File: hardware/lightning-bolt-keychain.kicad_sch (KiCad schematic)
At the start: 8 parts, among them SW1 SPST

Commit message: Repair KiCad PCB and update parts notes
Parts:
- BT1: value CR2032 -> CR1220/CR1225; symbol Battery:Battery_Cell -> Device:Battery_Cell
- SW1: footprint Button_Switch_SMD:SW_SPST_EVQP2 -> Button_Switch_SMD:SW_SPST_EVQP2_ShortPushTravel_H2.1mm
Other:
- note added: "Simple 12 mm coin-cell keychain circuit: BT1 -> SW1 -> three resistor/LED branches."
- note removed: "Simple CR2032 keychain circuit: BT1 -> SW1 -> three resistor/LED branches."
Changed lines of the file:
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@@
     (rev "A")
     (company "Open hardware concept")
-    (comment 1 "CR2032 powered amber LED keychain")
+    (comment 1 "12mm coin-cell powered amber LED keychain")
   )
   (junction (at 74.93 67.31) (diameter 0) (color 0 0 0 0)
@@
     (stroke (width 0) (type default))
   )
-  (wire (pts (xy 74.93 67.31) (xy 86.36 67.31))
+  (wire (pts (xy 74.93 67.31) (xy 87.63 67.31))
     (stroke (width 0) (type default))
   )
@@
     (stroke (width 0) (type default))
   )
-  (wire (pts (xy 74.93 85.09) (xy 86.36 85.09))
+  (wire (pts (xy 74.93 85.09) (xy 87.63 85.09))
     (stroke (width 0) (type default))
   )
@@
     (stroke (width 0) (type default))
   )
-  (wire (pts (xy 74.93 102.87) (xy 86.36 102.87))
+  (wire (pts (xy 74.93 102.87) (xy 87.63 102.87))
     (stroke (width 0) (type default))
   )
-  (wire (pts (xy 96.52 67.31) (xy 106.68 67.31))
+  (wire (pts (xy 95.25 67.31) (xy 107.95 67.31))
     (stroke (width 0) (type default))
   )
-  (wire (pts (xy 96.52 85.09) (xy 106.68 85.09))
+  (wire (pts (xy 95.25 85.09) (xy 107.95 85.09))
     (stroke (width 0) (type default))
   )
-  (wire (pts (xy 96.52 102.87) (xy 106.68 102.87))
+  (wire (pts (xy 95.25 102.87) (xy 107.95 102.87))
     (stroke (width 0) (type default))
   )
-  (wire (pts (xy 116.84 67.31) (xy 116.84 102.87))
+  (wire (pts (xy 115.57 67.31) (xy 115.57 102.87))
     (stroke (width 0) (type default))
   )
-  (wire (pts (xy 106.68 67.31) (xy 116.84 67.31))
+  (wire (pts (xy 115.57 67.31) (xy 115.57 67.31))
     (stroke (width 0) (type default))
   )
-  (wire (pts (xy 106.68 85.09) (xy 116.84 85.09))
+  (wire (pts (xy 115.57 85.09) (xy 115.57 85.09))
     (stroke (width 0) (type default))
   )
-  (wire (pts (xy 106.68 102.87) (xy 116.84 102.87))
+  (wire (pts (xy 115.57 102.87) (xy 115.57 102.87))
     (stroke (width 0) (type default))
   )
-  (symbol (lib_id "Battery:Battery_Cell") (at 35.56 67.31 0) (unit 1)
+  (global_label "GND" (shape input) (at 43.18 59.69 180)
+    (effects (font (size 1.27 1.27)) (justify right))
+  )
+  (global_label "GND" (shape input) (at 115.57 85.09 0)
+    (effects (font (size 1.27 1.27)) (justify left))
+  )
+  (symbol (lib_id "Device:Battery_Cell") (at 43.18 62.23 0) (unit 1)
     (in_bom yes) (on_board yes) (dnp no)
-    (property "Reference" "BT1" (at 35.56 60.96 0)
+    (property "Reference" "BT1" (at 45.72 64.77 0)
       (effects (font (size 1.27 1.27)))
     )
-    (property "Value" "CR2032" (at 35.56 73.66 0)
+    (property "Value" "CR1220/CR1225" (at 45.72 62.23 0)
       (effects (font (size 1.27 1.27)))
     )
-    (property "Footprint" "Battery:BatteryHolder_Keystone_3000_1x12mm" (at 35.56 67.31 0)
+    (property "Footprint" "Battery:BatteryHolder_Keystone_3000_1x12mm" (at 43.18 62.23 0)
       (effects (font (size 1.27 1.27)) hide)
     )
@@
       (effects (font (size 1.27 1.27)))
     )
-    (property "Footprint" "Button_Switch_SMD:SW_SPST_EVQP2" (at 58.42 67.31 0)
+    (property "Footprint" "Button_Switch_SMD:SW_SPST_EVQP2_ShortPushTravel_H2.1mm" (at 58.42 67.31 0)
       (effects (font (size 1.27 1.27)) hide)
     )
@@
     )
   )
-  (symbol (lib_id "Device:LED") (at 111.76 67.31 0) (unit 1)
+  (symbol (lib_id "Device:LED") (at 111.76 67.31 180) (unit 1)
     (in_bom yes) (on_board yes) (dnp no)
     (property "Reference" "D1" (at 111.76 60.96 0)
@@
     )
   )
-  (symbol (lib_id "Device:LED") (at 111.76 85.09 0) (unit 1)
+  (symbol (lib_id "Device:LED") (at 111.76 85.09 180) (unit 1)
     (in_bom yes) (on_board yes) (dnp no)
     (property "Reference" "D2" (at 111.76 78.74 0)
@@
     )
   )
-  (symbol (lib_id "Device:LED") (at 111.76 102.87 0) (unit 1)
+  (symbol (lib_id "Device:LED") (at 111.76 102.87 180) (unit 1)
     (in_bom yes) (on_board yes) (dnp no)
     (property "Reference" "D3" (at 111.76 96.52 0)
@@
     )
   )
-  (text "Simple CR2032 keychain circuit: BT1 -> SW1 -> three resistor/LED branches." (at 38.10 38.10 0)
+  (text "Simple 12 mm coin-cell keychain circuit: BT1 -> SW1 -> three resistor/LED branches." (at 38.10 38.10 0)
     (effects (font (size 1.27 1.27)) (justify left))
   )

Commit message: Clean up KiCad schematic and PCB visuals
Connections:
- net GND: now also BT1.2 (-), D1.1 (K), D2.1 (K), D3.1 (K)
- new net +BATT: BT1.1 (+), SW1.1 (A)
- new net LED1: D1.2 (A), R1.2
- new net LED2: D2.2 (A), R2.2
- new net LED3: D3.2 (A), R3.2
- new net VLED: R1.1, R2.1, R3.1, SW1.2 (B)
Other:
- note added: "12 mm coin-cell keychain circuit: BT1 -> SW1 -> three resistor/LED branches."
- note removed: "Simple 12 mm coin-cell keychain circuit: BT1 -> SW1 -> three resistor/LED branches."
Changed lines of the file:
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@@
     (comment 1 "12mm coin-cell powered amber LED keychain")
   )
-  (junction (at 74.93 67.31) (diameter 0) (color 0 0 0 0)
-  )
-  (junction (at 74.93 85.09) (diameter 0) (color 0 0 0 0)
-  )
-  (wire (pts (xy 43.18 67.31) (xy 53.34 67.31))
-    (stroke (width 0) (type default))
-  )
-  (wire (pts (xy 63.50 67.31) (xy 74.93 67.31))
-    (stroke (width 0) (type default))
-  )
-  (wire (pts (xy 74.93 67.31) (xy 87.63 67.31))
-    (stroke (width 0) (type default))
-  )
-  (wire (pts (xy 74.93 67.31) (xy 74.93 85.09))
-    (stroke (width 0) (type default))
-  )
-  (wire (pts (xy 74.93 85.09) (xy 87.63 85.09))
-    (stroke (width 0) (type default))
-  )
-  (wire (pts (xy 74.93 85.09) (xy 74.93 102.87))
-    (stroke (width 0) (type default))
-  )
-  (wire (pts (xy 74.93 102.87) (xy 87.63 102.87))
-    (stroke (width 0) (type default))
-  )
-  (wire (pts (xy 95.25 67.31) (xy 107.95 67.31))
-    (stroke (width 0) (type default))
-  )
-  (wire (pts (xy 95.25 85.09) (xy 107.95 85.09))
-    (stroke (width 0) (type default))
-  )
-  (wire (pts (xy 95.25 102.87) (xy 107.95 102.87))
-    (stroke (width 0) (type default))
-  )
-  (wire (pts (xy 115.57 67.31) (xy 115.57 102.87))
-    (stroke (width 0) (type default))
-  )
-  (wire (pts (xy 115.57 67.31) (xy 115.57 67.31))
-    (stroke (width 0) (type default))
-  )
-  (wire (pts (xy 115.57 85.09) (xy 115.57 85.09))
-    (stroke (width 0) (type default))
-  )
-  (wire (pts (xy 115.57 102.87) (xy 115.57 102.87))
-    (stroke (width 0) (type default))
-  )
-  (global_label "GND" (shape input) (at 43.18 59.69 180)
+  (global_label "+BATT" (shape input) (at 43.18 38.10 90)
     (effects (font (size 1.27 1.27)) (justify right))
   )
-  (global_label "GND" (shape input) (at 115.57 85.09 0)
+  (global_label "GND" (shape input) (at 43.18 45.72 270)
+    (effects (font (size 1.27 1.27)) (justify right))
+  )
+  (global_label "+BATT" (shape input) (at 53.34 38.10 180)
+    (effects (font (size 1.27 1.27)) (justify right))
+  )
+  (global_label "VLED" (shape input) (at 63.50 38.10 0)
     (effects (font (size 1.27 1.27)) (justify left))
   )
-  (symbol (lib_id "Device:Battery_Cell") (at 43.18 62.23 0) (unit 1)
+  (global_label "VLED" (shape input) (at 87.63 60.96 180)
+    (effects (font (size 1.27 1.27)) (justify right))
+  )
+  (global_label "LED1" (shape input) (at 95.25 60.96 0)
+    (effects (font (size 1.27 1.27)) (justify left))
+  )
+  (global_label "LED1" (shape input) (at 107.95 60.96 180)
+    (effects (font (size 1.27 1.27)) (justify right))
+  )
+  (global_label "GND" (shape input) (at 115.57 60.96 0)
+    (effects (font (size 1.27 1.27)) (justify left))
+  )
+  (global_label "VLED" (shape input) (at 87.63 78.74 180)
+    (effects (font (size 1.27 1.27)) (justify right))
+  )
+  (global_label "LED2" (shape input) (at 95.25 78.74 0)
+    (effects (font (size 1.27 1.27)) (justify left))
+  )
+  (global_label "LED2" (shape input) (at 107.95 78.74 180)
+    (effects (font (size 1.27 1.27)) (justify right))
+  )
+  (global_label "GND" (shape input) (at 115.57 78.74 0)
+    (effects (font (size 1.27 1.27)) (justify left))
+  )
+  (global_label "VLED" (shape input) (at 87.63 96.52 180)
+    (effects (font (size 1.27 1.27)) (justify right))
+  )
+  (global_label "LED3" (shape input) (at 95.25 96.52 0)
+    (effects (font (size 1.27 1.27)) (justify left))
+  )
+  (global_label "LED3" (shape input) (at 107.95 96.52 180)
+    (effects (font (size 1.27 1.27)) (justify right))
+  )
+  (global_label "GND" (shape input) (at 115.57 96.52 0)
+    (effects (font (size 1.27 1.27)) (justify left))
+  )
+  (symbol (lib_id "Device:Battery_Cell") (at 43.18 43.18 0) (unit 1)
     (in_bom yes) (on_board yes) (dnp no)
-    (property "Reference" "BT1" (at 45.72 64.77 0)
+    (property "Reference" "BT1" (at 43.18 36.83 0)
       (effects (font (size 1.27 1.27)))
     )
-    (property "Value" "CR1220/CR1225" (at 45.72 62.23 0)
+    (property "Value" "CR1220/CR1225" (at 43.18 49.53 0)
       (effects (font (size 1.27 1.27)))
     )
-    (property "Footprint" "Battery:BatteryHolder_Keystone_3000_1x12mm" (at 43.18 62.23 0)
+    (property "Footprint" "Battery:BatteryHolder_Keystone_3000_1x12mm" (at 43.18 43.18 0)
       (effects (font (size 1.27 1.27)) hide)
     )
   )
-  (symbol (lib_id "Switch:SW_SPST") (at 58.42 67.31 0) (unit 1)
+  (symbol (lib_id "Switch:SW_SPST") (at 58.42 38.10 0) (unit 1)
     (in_bom yes) (on_board yes) (dnp no)
-    (property "Reference" "SW1" (at 58.42 60.96 0)
+    (property "Reference" "SW1" (at 58.42 31.75 0)
       (effects (font (size 1.27 1.27)))
     )
-    (property "Value" "SPST" (at 58.42 73.66 0)
+    (property "Value" "SPST" (at 58.42 44.45 0)
       (effects (font (size 1.27 1.27)))
     )
-    (property "Footprint" "Button_Switch_SMD:SW_SPST_EVQP2_ShortPushTravel_H2.1mm" (at 58.42 67.31 0)
+    (property "Footprint" "Button_Switch_SMD:SW_SPST_EVQP2_ShortPushTravel_H2.1mm" (at 58.42 38.10 0)
       (effects (font (size 1.27 1.27)) hide)
     )
   )
-  (symbol (lib_id "Device:R") (at 91.44 67.31 90) (unit 1)
+  (symbol (lib_id "Device:R") (at 91.44 60.96 90) (unit 1)
     (in_bom yes) (on_board yes) (dnp no)
-    (property "Reference" "R1" (at 91.44 62.23 90)
+    (property "Reference" "R1" (at 91.44 54.61 90)
       (effects (font (size 1.27 1.27)))
     )
-    (property "Value" "220" (at 91.44 72.39 90)
+    (property "Value" "220" (at 91.44 67.31 90)
       (effects (font (size 1.27 1.27)))
     )
-    (property "Footprint" "Resistor_SMD:R_0603_1608Metric" (at 91.44 67.31 0)
+    (property "Footprint" "Resistor_SMD:R_0603_1608Metric" (at 91.44 60.96 0)
       (effects (font (size 1.27 1.27)) hide)
     )
   )
-  (symbol (lib_id "Device:R") (at 91.44 85.09 90) (unit 1)
+  (symbol (lib_id "Device:R") (at 91.44 78.74 90) (unit 1)
     (in_bom yes) (on_board yes) (dnp no)
-    (property "Reference" "R2" (at 91.44 80.01 90)
+    (property "Reference" "R2" (at 91.44 72.39 90)
       (effects (font (size 1.27 1.27)))
     )
-    (property "Value" "220" (at 91.44 90.17 90)
+    (property "Value" "220" (at 91.44 85.09 90)
       (effects (font (size 1.27 1.27)))
     )
-    (property "Footprint" "Resistor_SMD:R_0603_1608Metric" (at 91.44 85.09 0)
+    (property "Footprint" "Resistor_SMD:R_0603_1608Metric" (at 91.44 78.74 0)
       (effects (font (size 1.27 1.27)) hide)
     )
   )
-  (symbol (lib_id "Device:R") (at 91.44 102.87 90) (unit 1)
+  (symbol (lib_id "Device:R") (at 91.44 96.52 90) (unit 1)
     (in_bom yes) (on_board yes) (dnp no)
-    (property "Reference" "R3" (at 91.44 97.79 90)
+    (property "Reference" "R3" (at 91.44 90.17 90)
       (effects (font (size 1.27 1.27)))
     )
-    (property "Value" "220" (at 91.44 107.95 90)
+    (property "Value" "220" (at 91.44 102.87 90)
       (effects (font (size 1.27 1.27)))
     )
-    (property "Footprint" "Resistor_SMD:R_0603_1608Metric" (at 91.44 102.87 0)
+    (property "Footprint" "Resistor_SMD:R_0603_1608Metric" (at 91.44 96.52 0)
       (effects (font (size 1.27 1.27)) hide)
     )
   )
-  (symbol (lib_id "Device:LED") (at 111.76 67.31 180) (unit 1)
+  (symbol (lib_id "Device:LED") (at 111.76 60.96 180) (unit 1)
     (in_bom yes) (on_board yes) (dnp no)
-    (property "Reference" "D1" (at 111.76 60.96 0)
+    (property "Reference" "D1" (at 111.76 54.61 180)
       (effects (font (size 1.27 1.27)))
     )
-    (property "Value" "Amber" (at 111.76 73.66 0)
+    (property "Value" "Amber" (at 111.76 67.31 180)
       (effects (font (size 1.27 1.27)))
     )
-    (property "Footprint" "LED_SMD:LED_0603_1608Metric" (at 111.76 67.31 0)
+    (property "Footprint" "LED_SMD:LED_0603_1608Metric" (at 111.76 60.96 0)
       (effects (font (size 1.27 1.27)) hide)
     )
   )
-  (symbol (lib_id "Device:LED") (at 111.76 85.09 180) (unit 1)
+  (symbol (lib_id "Device:LED") (at 111.76 78.74 180) (unit 1)
     (in_bom yes) (on_board yes) (dnp no)
-    (property "Reference" "D2" (at 111.76 78.74 0)
+    (property "Reference" "D2" (at 111.76 72.39 180)
       (effects (font (size 1.27 1.27)))
     )
-    (property "Value" "Amber" (at 111.76 91.44 0)
+    (property "Value" "Amber" (at 111.76 85.09 180)
       (effects (font (size 1.27 1.27)))
     )
-    (property "Footprint" "LED_SMD:LED_0603_1608Metric" (at 111.76 85.09 0)
+    (property "Footprint" "LED_SMD:LED_0603_1608Metric" (at 111.76 78.74 0)
       (effects (font (size 1.27 1.27)) hide)
     )
   )
-  (symbol (lib_id "Device:LED") (at 111.76 102.87 180) (unit 1)
+  (symbol (lib_id "Device:LED") (at 111.76 96.52 180) (unit 1)
     (in_bom yes) (on_board yes) (dnp no)
-    (property "Reference" "D3" (at 111.76 96.52 0)
+    (property "Reference" "D3" (at 111.76 90.17 180)
       (effects (font (size 1.27 1.27)))
     )
-    (property "Value" "Amber" (at 111.76 109.22 0)
+    (property "Value" "Amber" (at 111.76 102.87 180)
       (effects (font (size 1.27 1.27)))
     )
-    (property "Footprint" "LED_SMD:LED_0603_1608Metric" (at 111.76 102.87 0)
+    (property "Footprint" "LED_SMD:LED_0603_1608Metric" (at 111.76 96.52 0)
       (effects (font (size 1.27 1.27)) hide)
     )
   )
-  (text "Simple 12 mm coin-cell keychain circuit: BT1 -> SW1 -> three resistor/LED branches." (at 38.10 38.10 0)
+  (text "12 mm coin-cell keychain circuit: BT1 -> SW1 -> three resistor/LED branches." (at 35.56 25.40 0)
     (effects (font (size 1.27 1.27)) (justify left))
   )

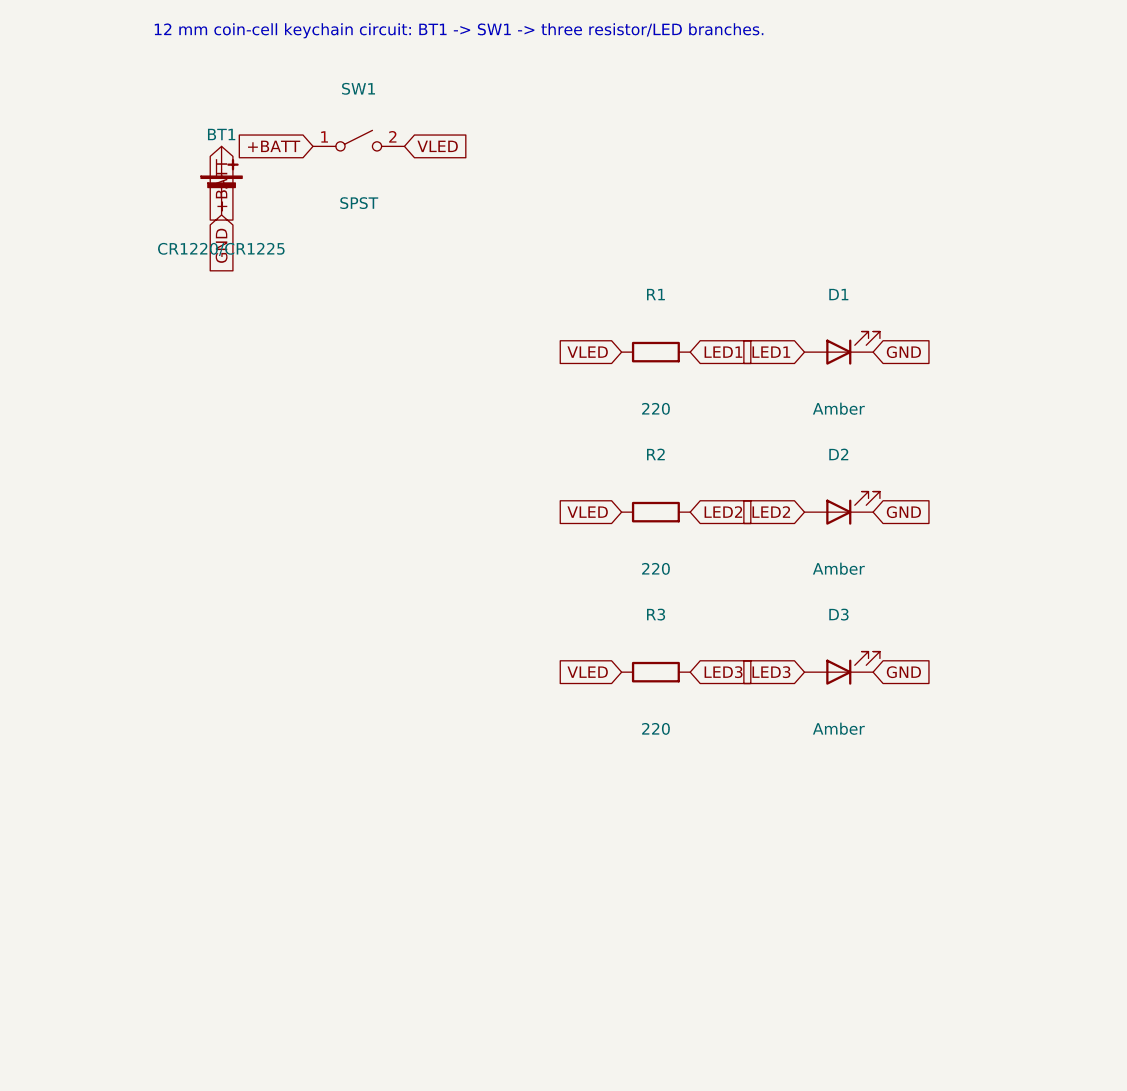
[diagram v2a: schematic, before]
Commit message: Convert keychain to USB-C powered design
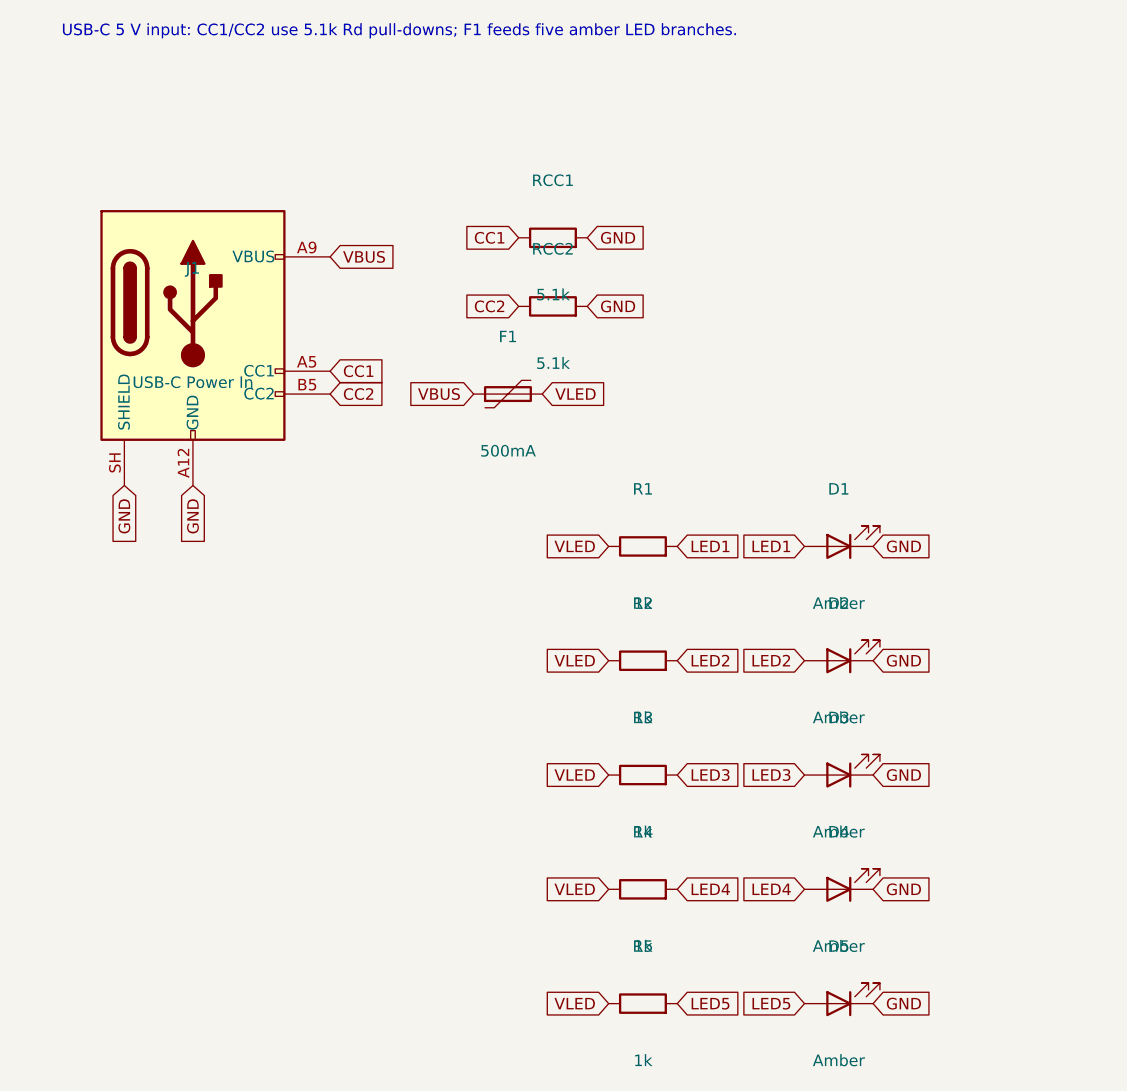
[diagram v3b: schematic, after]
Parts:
- removed BT1: CR1220/CR1225, Battery:BatteryHolder_Keystone_3000_1x12mm, symbol Device:Battery_Cell
- removed SW1: SPST, Button_Switch_SMD:SW_SPST_EVQP2_ShortPushTravel_H2.1mm, symbol Switch:SW_SPST
- added D4, D5: Amber, LED_SMD:LED_0603_1608Metric, symbol Device:LED
- added F1: 500mA, Fuse:Fuse_1206_3216Metric, symbol Device:Polyfuse
- added J1: USB-C Power In, Connector_USB:USB_C_Receptacle_GCT_USB4125-xx-x_6P_TopMnt_Horizontal, symbol Connector:USB_C_Receptacle_PowerOnly_6P
- added R4, R5: 1k, Resistor_SMD:R_0603_1608Metric, symbol Device:R
- added RCC1, RCC2: 5.1k, Resistor_SMD:R_0603_1608Metric, symbol Device:R
- R1, R2, R3: value 220 -> 1k
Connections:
- net GND: now also D4.1 (K), D5.1 (K), J1.A12 (GND), J1.B12 (GND), J1.SH (SHIELD), RCC1.2, RCC2.2
- net VLED: now also F1.2, R4.1, R5.1
- new net CC1: J1.A5 (CC1), RCC1.1
- new net CC2: J1.B5 (CC2), RCC2.1
- new net LED4: D4.2 (A), R4.2
- new net LED5: D5.2 (A), R5.2
- new net VBUS: F1.1, J1.A9 (VBUS), J1.B9 (VBUS)
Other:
- note added: "USB-C 5 V input: CC1/CC2 use 5.1k Rd pull-downs; F1 feeds five amber LED branches."
- note removed: "12 mm coin-cell keychain circuit: BT1 -> SW1 -> three resistor/LED branches."
- title: Lightning Bolt PCB Keychain -> USB-C Lightning Bolt PCB Keychain
